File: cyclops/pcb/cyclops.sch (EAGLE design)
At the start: 180 parts, among them Q1 SSM3K324, Q2 SSM3K324, Q3 SSM3K324, Q4 IRF510, U1 MCP4921, U10 ADG1201, U11 THS4281, U12 MAX4564, U13 ZXTD, U14 ZXTD, U15 OPA1664, U2 LT1931, U3 LT1764A, U31 TPS62153, U4 BD00IA5WEFJ-E2, U5 TPS72325, U6 LT1711, U7 TLV3701, U8 ADR03, U9 LT1880

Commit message: Silkscreen work.
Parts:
- U4: value BD00IA5WEFJ-E2 -> BD00IA5WEFJ
- VPRE: device cyclops:TPTP16R -> jonnew:TP_RC0603
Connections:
- removed net N$57: C24.2
- net GND: now also C24.2
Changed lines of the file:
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@@
 <part name="-5V" library="jonnew" deviceset="TP" device="_RC0603" value="RCU-0C"/>
 <part name="-2.5V" library="jonnew" deviceset="TP" device="_RC0603" value="RCU-0C"/>
-<part name="VPRE" library="cyclops" deviceset="TP" device="TP16R" value="TPTP16R"/>
+<part name="VPRE" library="jonnew" deviceset="TP" device="_RC0603" value="TPTP16R"/>
 <part name="C27" library="cyclops" deviceset="C" device="_0603" value="0.1uF"/>
 <part name="C28" library="cyclops" deviceset="C" device="_0603" value="0.1uF"/>
@@
 <part name="R6" library="jonnew" deviceset="R" device="_1206" value="50"/>
 <part name="R7" library="jonnew" deviceset="R" device="_1206" value="50"/>
-<part name="U4" library="jonnew" deviceset="LDO_ADJUST" device="_BDXXFC0" value="BD00IA5WEFJ-E2"/>
+<part name="U4" library="jonnew" deviceset="LDO_ADJUST" device="_BDXXFC0" value="BD00IA5WEFJ"/>
 <part name="P+8" library="cyclops" deviceset="+5V" device="" value="+5V"/>
 <part name="P+16" library="jonnew" deviceset="+5V" device="" value="+6V"/>
@@
 <wire x1="5.08" y1="-35.56" x2="5.08" y2="-27.94" width="0.1524" layer="91"/>
 </segment>
+<segment>
+<pinref part="C24" gate="C" pin="2"/>
+<wire x1="15.24" y1="-2.54" x2="15.24" y2="-5.08" width="0.1524" layer="91"/>
+</segment>
 </net>
 <net name="N$6" class="0">
@@
 </segment>
 </net>
-<net name="N$57" class="0">
-<segment>
-<pinref part="C24" gate="C" pin="2"/>
-<wire x1="15.24" y1="-2.54" x2="15.24" y2="-5.08" width="0.1524" layer="91"/>
-</segment>
-</net>

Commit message: Silkscreen nearly done. Final check and then time for fab.
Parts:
- removed C43: 22uF, jonnew:C_0805
- added C40: 22uF, cyclops:C_1210
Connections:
- net +5V: now also C40.1; no longer C43.1
- net GND: now also C40.2; no longer C43.2
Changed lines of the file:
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@@
 <part name="C41" library="jonnew" deviceset="C" device="_1206" value="10uF"/>
 <part name="C42" library="jonnew" deviceset="C" device="_0603" value="3.3nF"/>
-<part name="C43" library="jonnew" deviceset="C" device="_0805" value="22uF"/>
 <part name="U$31" library="cyclops" deviceset="GND1" device=""/>
 <part name="U$74" library="cyclops" deviceset="GND1" device=""/>
@@
 <part name="U$79" library="cyclops" deviceset="GND2" device=""/>
 <part name="+13.3V" library="jonnew" deviceset="TP" device="_RC0603" value="RCU-0C"/>
+<part name="C40" library="cyclops" deviceset="C" device="_1210" value="22uF"/>
 </parts>
 <sheets>
@@
 <instance part="C41" gate="C" x="-78.74" y="-50.8"/>
 <instance part="C42" gate="C" x="-58.42" y="-58.42"/>
-<instance part="C43" gate="C" x="30.48" y="-48.26"/>
 <instance part="U$31" gate="G$1" x="-5.08" y="-71.12"/>
 <instance part="U$74" gate="G$1" x="-45.72" y="-71.12"/>
@@
 <instance part="R52" gate="R" x="114.3" y="10.16" rot="R90"/>
 <instance part="+13.3V" gate="G$1" x="7.62" y="43.18"/>
+<instance part="C40" gate="C" x="30.48" y="-48.26"/>
 </instances>
 <busses>
@@
 </segment>
 <segment>
-<pinref part="C43" gate="C" pin="2"/>
 <wire x1="30.48" y1="-53.34" x2="30.48" y2="-68.58" width="0.1524" layer="91"/>
+<pinref part="C40" gate="C" pin="2"/>
 </segment>
 </net>
@@
 <pinref part="+5V" gate="G$1" pin="TP"/>
 <junction x="30.48" y="-38.1"/>
-<pinref part="C43" gate="C" pin="1"/>
 <wire x1="30.48" y1="-38.1" x2="30.48" y2="-45.72" width="0.1524" layer="91"/>
-</segment>
-</net>
+<pinref part="C40" gate="C" pin="1"/>
+</segment>
+</net>

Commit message: Very close to finished with Rev. 3.6-beta PCB
- A couple lingering TODOs as stated on the first page of the schematic.
  Mostly mechnical/overlap issues at this point
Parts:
- VREF<>TTL: value JS102 -> AS12AC
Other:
- note added: "TODO: 1. ~~Replace arduino headers with teensy headers (male and female since teensy comes without them)~~ 2. ~~Are the LED arrays mounted at correct distance from board edge?~~ 3.~~ Is teensy at correct distance from board edge?~~ 4. ~~Is there adequare clearance b/w rear panel mount components~~ 5. Rearrange panels to fit changes in front and back 6. ~~+5V regulator layou EDIT: +6V~~ 7. ~~Test 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"
- note removed: "TODO: 1. ~~Replace arduino headers with teensy headers (male and female since teensy comes without them)~~ 2. ~~Are the LED arrays mounted at correct distance from board edge?~~ 3.~~ Is teensy at correct distance from board edge?~~ 4. Is there adequare clearance b/w rear panel mount components 5. Rearrange panels to fit changes in front and back 6. +5V regulator layout 7. ~~Test LED ON circuit. Y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"
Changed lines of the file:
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@@
 <part name="OC" library="jonnew" deviceset="LED_2X" device="_VERTICAL" value="569-0112-200"/>
 <part name="D2" library="jonnew" deviceset="S-DIODE" device="SOD-123" value="1N5819"/>
-<part name="VREF&lt;&gt;TTL" library="jonnew" deviceset="SPDT" device="_AS12A*" value="JS102"/>
+<part name="VREF&lt;&gt;TTL" library="jonnew" deviceset="SPDT" device="_AS12A*" value="AS12AC"/>
 <part name="C20" library="cyclops" deviceset="C" device="_0603" value=".1uF"/>
 <part name="R27" library="cyclops" deviceset="R" device="_0603" value="1k"/>
@@
 <wire x1="17.78" y1="17.78" x2="17.78" y2="99.06" width="0.4064" layer="97" style="shortdash"/>
 <wire x1="17.78" y1="99.06" x2="-7.62" y2="99.06" width="0.4064" layer="97" style="shortdash"/>
-<text x="76.2" y="162.56" size="2.54" layer="97">TODO:
+<text x="76.2" y="149.86" size="2.54" layer="97">TODO:
 1. ~~Replace arduino headers with teensy headers (male and female since teensy comes without them)~~
 2. ~~Are the LED arrays mounted at correct distance from board edge?~~
 3.~~ Is teensy at correct distance from board edge?~~
-4. Is there adequare clearance b/w rear panel mount components
+4. ~~Is there adequare clearance b/w rear panel mount components~~
 5. Rearrange panels to fit changes in front and back
-6. +5V regulator layout
+6. ~~+5V regulator layou EDIT: +6V~~
 7. ~~Test LED ON circuit. You will at least have to replace the N BJT with an P BJT since LED ON is inverted.~~
 8. ~~Teensy itself will need to be modified with cut trace and schottky diode to work with external power~~
 9. ~~Replace SMD VREF/TTL switch with vertical slide like 360‑3344‑ND~~
 10. ~~Bring +12V up to +13.5 and -1.5 to -2.5V if possible. Examine components to see what is limiting the positive/negative rails.~~
-11. Stripline calculations and proper terminations for new high-side analog drive train and new analog switch (thinking about replacing drive train MAX4564 with ADV3220 which provides 800 MHz -3dB and 2x gain hardcoded). EDIT: 11 mil is good when using top layer and 2nd layer ground for circuit hub PCBs
-12. Rename jumper resistors
-13. Replace +6V LDO with something that can actually handle +13.3V input. Place close to 13.3V LDO. Add buck converter to digital power supply to provide fixed 5V for teensy and to power inverter. 15V should be routed to digital section on bottom layer of board along the bottom edge of board. Ground should be cut along the top edge of this trace to force digital power return back to 15V jack along this trace, away from analog stuff.
-14. ~~Protect inputs of opa1664 with schottkys~~</text>
+11. ~~Stripline calculations and proper terminations for new high-side analog drive train and new analog switch (thinking about replacing drive train MAX4564 with ADV3220 which provides 800 MHz -3dB and 2x gain hardcoded). EDIT: 11 mil is good when using top layer and 2nd layer ground for circuit hub PCBs~~
+12. ~~Rename jumper resistors~~
+13. ~~Replace +6V LDO with something that can actually handle +13.3V input. Place close to 13.3V LDO. Add buck converter to digital power supply to provide fixed 5V for teensy and to power inverter. 15V should be routed to digital section on bottom layer of board along the bottom edge of board. Ground should be cut along the top edge of this trace to force digital power return back to 15V jack along this trace, away from analog stuff.~~
+14. ~~Protect inputs of opa1664 with schottkys~~
+15. TTL/VREF switch pin overlaps with heatsink.
+16. Remove unused vref pin from teensy so that thta TRIG BNC has plenty of room. Update the headers to be 2 pin instead of 3</text>
 <wire x1="-12.7" y1="190.5" x2="71.12" y2="190.5" width="0.4064" layer="97" style="shortdash"/>
 <wire x1="71.12" y1="190.5" x2="71.12" y2="149.86" width="0.4064" layer="97" style="shortdash"/>
@@
 <instance part="Q3" gate="G$1" x="78.74" y="71.12"/>
 <instance part="Q2" gate="G$1" x="17.78" y="-30.48"/>
-<instance part="P-8" gate="1" x="-35.56" y="-53.34"/>
+<instance part="P-8" gate="1" x="-35.56" y="-60.96"/>
 <instance part="C21" gate="C" x="-30.48" y="-43.18" rot="MR270"/>
-<instance part="U$71" gate="G$1" x="-22.86" y="-50.8" rot="MR0"/>
+<instance part="U$71" gate="G$1" x="-22.86" y="-60.96" rot="MR0"/>
 <instance part="R25" gate="R" x="10.16" y="-40.64" smashed="yes" rot="R90">
 <attribute name="NAME" x="8.6614" y="-44.45" size="1.778" layer="95" rot="R90"/>
@@
 <instance part="U6" gate="G$1" x="-40.64" y="-30.48"/>
 <instance part="U6" gate="G$2" x="-38.1" y="-30.48"/>
-<instance part="U$77" gate="G$1" x="-43.18" y="-50.8" rot="MR0"/>
+<instance part="U$77" gate="G$1" x="-43.18" y="-60.96" rot="MR0"/>
 <instance part="P+9" gate="1" x="20.32" y="111.76"/>
 <instance part="P+10" gate="1" x="81.28" y="111.76"/>
@@
 <pinref part="C21" gate="C" pin="2"/>
 <wire x1="-25.4" y1="-43.18" x2="-22.86" y2="-43.18" width="0.1524" layer="91"/>
-<wire x1="-22.86" y1="-43.18" x2="-22.86" y2="-48.26" width="0.1524" layer="91"/>
+<wire x1="-22.86" y1="-43.18" x2="-22.86" y2="-58.42" width="0.1524" layer="91"/>
 </segment>
 <segment>
@@
 <wire x1="-43.18" y1="-45.72" x2="-43.18" y2="-43.18" width="0.1524" layer="91"/>
 <junction x="-43.18" y="-45.72"/>
-<wire x1="-43.18" y1="-45.72" x2="-43.18" y2="-48.26" width="0.1524" layer="91"/>
+<wire x1="-43.18" y1="-45.72" x2="-43.18" y2="-58.42" width="0.1524" layer="91"/>
 </segment>
 <segment>
@@
 <wire x1="-35.56" y1="-38.1" x2="-35.56" y2="-43.18" width="0.1524" layer="91"/>
 <pinref part="C21" gate="C" pin="1"/>
-<wire x1="-35.56" y1="-43.18" x2="-35.56" y2="-50.8" width="0.1524" layer="91"/>
+<wire x1="-35.56" y1="-43.18" x2="-35.56" y2="-58.42" width="0.1524" layer="91"/>
 <wire x1="-33.02" y1="-43.18" x2="-35.56" y2="-43.18" width="0.1524" layer="91"/>
 <junction x="-35.56" y="-43.18"/>

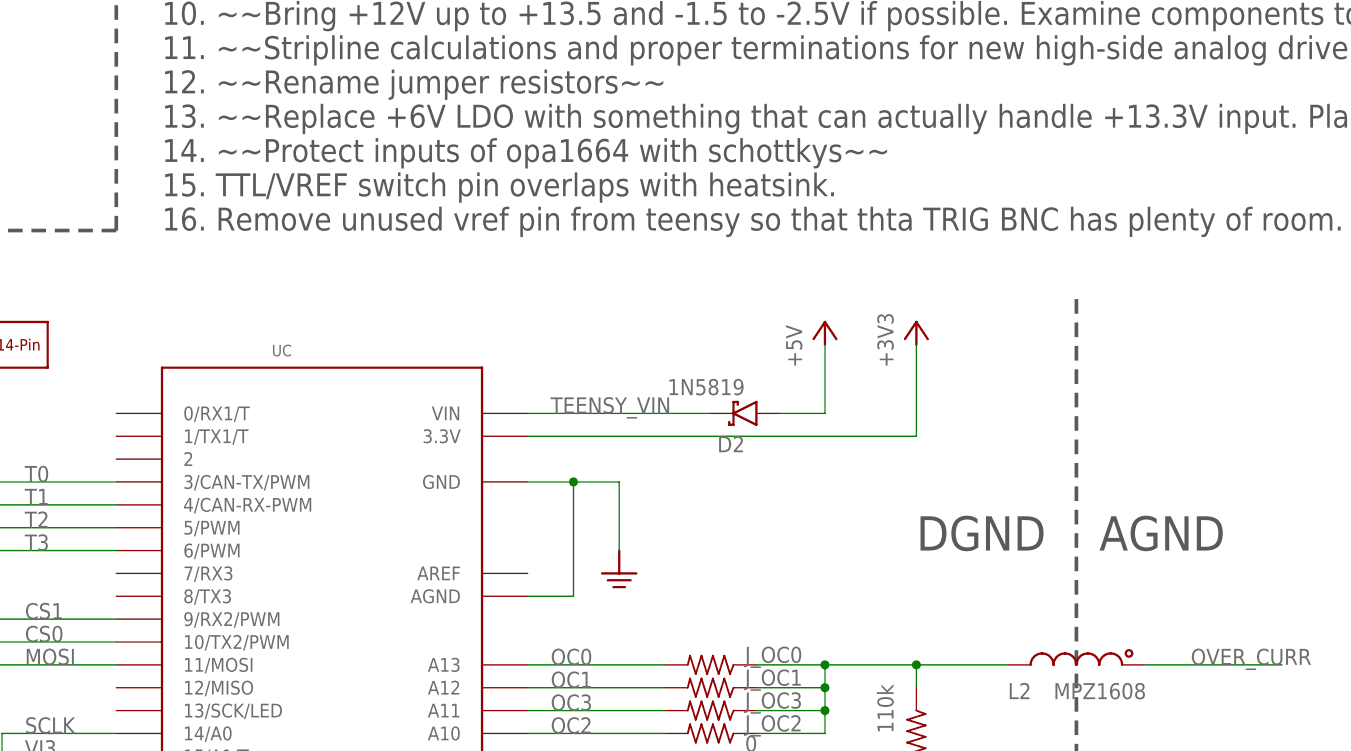
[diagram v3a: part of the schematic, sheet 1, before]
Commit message: Fixed heatsink overlap issue and removed teensy AREF
- Moved to 1.7in x 1.7in heatsink because the AREF/TTL switch had a
  through hole contact that would have overlapped with the 1.8in
  version.
- Teensy AREF pin was in the way of the TRIG BNC and not needed, so I
  removed it. BOM has yet to be updated (3 pin header --> 2 pin).
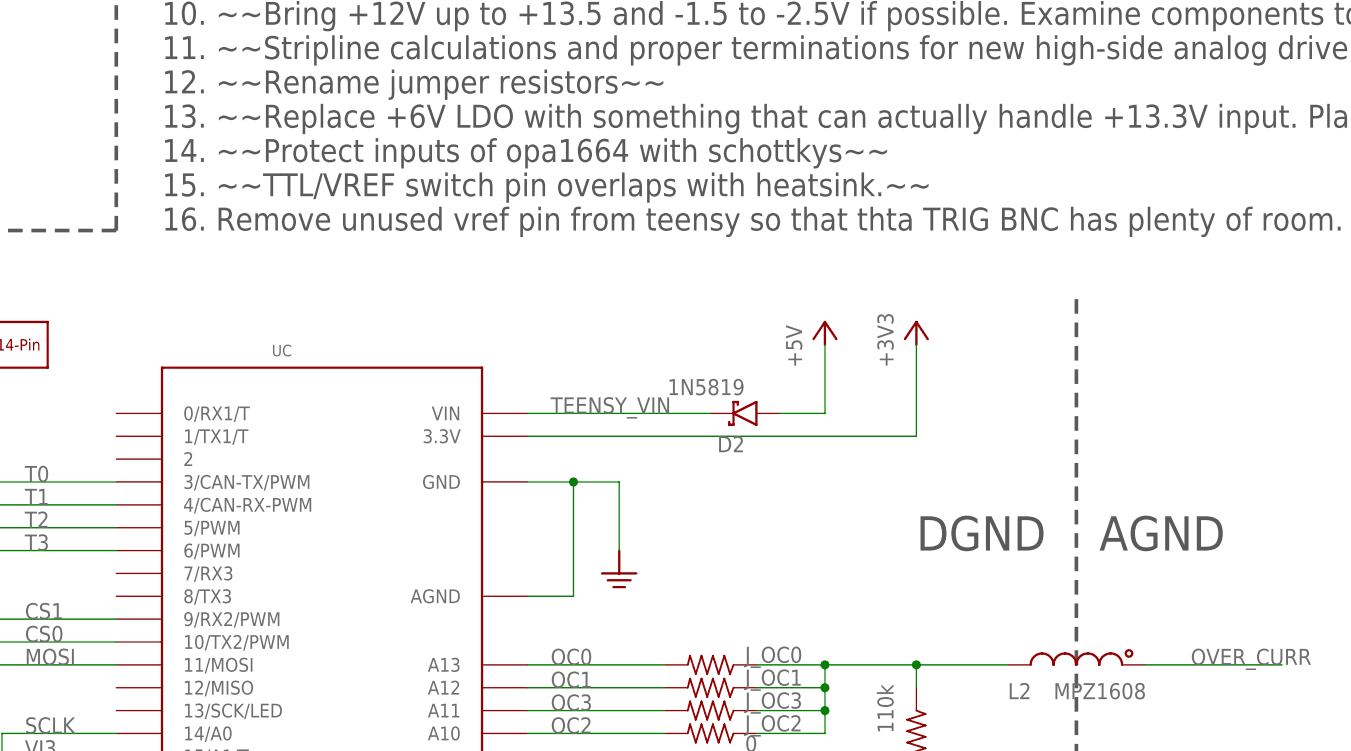
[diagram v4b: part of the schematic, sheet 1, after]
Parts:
- HEATSINK: value BDN18 -> BDN17; device cyclops:HEATSINK_BDN18 -> jonnew:HEATSINK_BDN17
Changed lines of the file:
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@@
 <part name="U$44" library="cyclops" deviceset="GND2" device=""/>
 <part name="U$46" library="cyclops" deviceset="GND2" device=""/>
-<part name="HEATSINK" library="cyclops" deviceset="HEATSINK" device="_BDN18" value="BDN18"/>
+<part name="HEATSINK" library="jonnew" deviceset="HEATSINK" device="_BDN17" value="BDN17"/>
 <part name="R36" library="cyclops" deviceset="R" device="_0603" value="0"/>
 <part name="R39" library="cyclops" deviceset="R" device="_0603"/>
@@
 13. ~~Replace +6V LDO with something that can actually handle +13.3V input. Place close to 13.3V LDO. Add buck converter to digital power supply to provide fixed 5V for teensy and to power inverter. 15V should be routed to digital section on bottom layer of board along the bottom edge of board. Ground should be cut along the top edge of this trace to force digital power return back to 15V jack along this trace, away from analog stuff.~~
 14. ~~Protect inputs of opa1664 with schottkys~~
-15. TTL/VREF switch pin overlaps with heatsink.
+15. ~~TTL/VREF switch pin overlaps with heatsink.~~
 16. Remove unused vref pin from teensy so that thta TRIG BNC has plenty of room. Update the headers to be 2 pin instead of 3</text>
 <wire x1="-12.7" y1="190.5" x2="71.12" y2="190.5" width="0.4064" layer="97" style="shortdash"/>
